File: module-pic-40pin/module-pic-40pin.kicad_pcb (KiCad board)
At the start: 2 copper layers, 93 x 61.9 mm, 21 parts, among them J1 input_power, J2 ANALOG, J3 icsp, J4 PORTB, J5 PORTC, J6 Conn_02x04_Odd_Even, J7 RB0_CONN, J8 PORTD, SW1 reset, SW2 EXT_INT0, U1 PIC16F877A-IP, Y1 20MHz

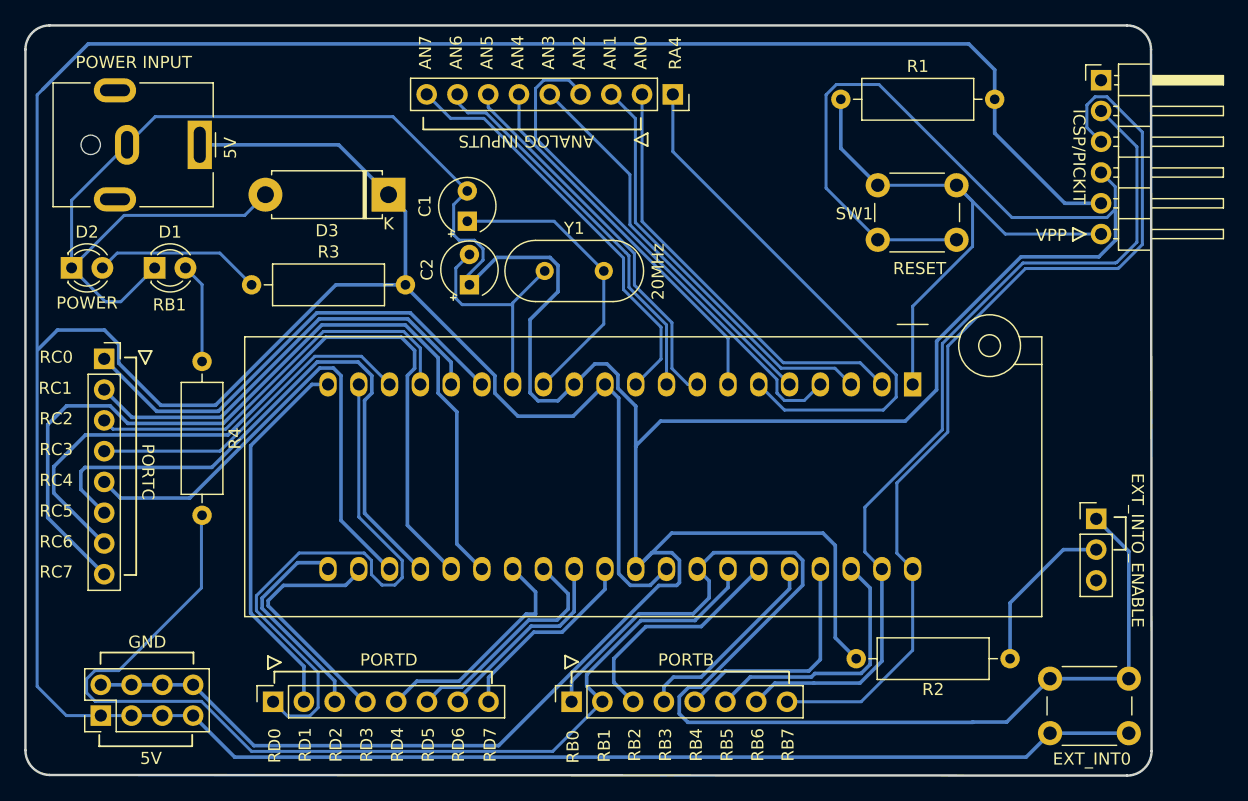
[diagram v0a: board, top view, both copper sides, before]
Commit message: update module-pic-40pin layout - v1.2
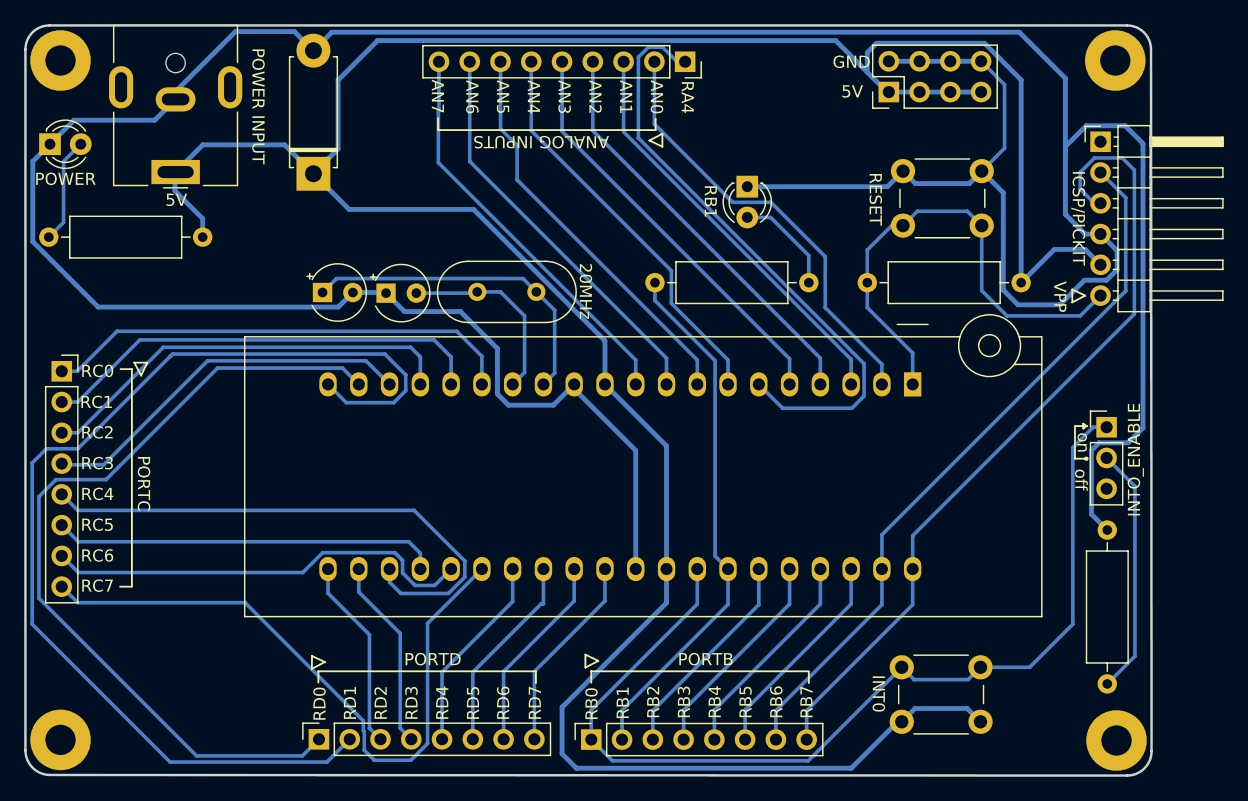
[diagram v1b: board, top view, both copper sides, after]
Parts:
- added REF**: MountingHole_2.5mm_Pad, MountingHole:MountingHole_2.5mm_Pad, F.Cu at (107.8, 69.6)
- added REF**: MountingHole_2.5mm_Pad, MountingHole:MountingHole_2.5mm_Pad, F.Cu at (195.0, 125.8)
- added REF**: MountingHole_2.5mm_Pad, MountingHole:MountingHole_2.5mm_Pad, F.Cu at (194.9, 69.6)
- added REF**: MountingHole_2.5mm_Pad, MountingHole:MountingHole_2.5mm_Pad, F.Cu at (107.8, 125.7)
- moved J6 83.0 mm to (176.2, 72.3)
- moved R4 50.5 mm to (169.6, 88.0), turned to 180 degrees
- moved D1 49.4 mm to (164.5, 80.1), turned to -90 degrees
- moved R3 17.2 mm to (106.8, 84.2)
- moved R1 15.3 mm to (174.4, 88.0)
- moved C1 13.3 mm to (129.4, 88.8), turned to 0 degrees
- moved SW2 12.3 mm to (177.2, 119.7)
- moved D2 10.4 mm to (106.9, 76.6)
- moved R2 8.29 mm to (194.2, 121.1), turned to 90 degrees
- moved J7 7.61 mm to (194.2, 99.9)
- moved SW1 7.19 mm to (177.3, 78.8), turned to 0 degrees
- moved C2 6.92 mm to (134.7, 88.8), turned to 0 degrees
- moved D3 6.43 mm to (128.7, 79.0), turned to 90 degrees
- moved Y1 5.83 mm to (142.2, 88.7)
- moved J3 5.08 mm to (193.6, 76.4)
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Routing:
- net +5V: track 348.2 -> 232.3 mm
- net /RD1: track 31.4 -> 89.0 mm
- net /RB1: track 85.0 -> 43.8 mm
- net GND: track 321.9 -> 293.8 mm
- net /RC6: track 62.5 -> 35.7 mm
- net /RD0: track 48.8 -> 68.8 mm
- net /RC5: track 50.5 -> 31.9 mm
- net /RB0: track 99.4 -> 81.8 mm
- net /RC7: track 71.2 -> 54.3 mm
- net /RB6: track 72.8 -> 59.6 mm
- net /RB7: track 77.9 -> 67.1 mm
- net /AN2: track 42.4 -> 34.4 mm
- net Net-(J7-Pad2): track 13.5 -> 20.6 mm
- net /VPP: track 47.5 -> 40.6 mm
- net Net-(D2-Pad2): track 13.9 -> 8.76 mm
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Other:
- board text added: "INT0"
- board text added: "INTO_ENABLE"
- board text added: "off"
- board text added: "on"
- board text removed: "EXT_INT0"
- board text removed: "EXT_INTO_ENABLE"

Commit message: update module-pic-40pin
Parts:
- added G***: LOGO, footprints:ladesi, F.Cu at (115.3, 120.1)
- added REF**: KiCad-Logo, Symbol:KiCad-Logo2_5mm_SilkScreen, F.Cu at (151.9, 81.1)
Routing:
- net /AN0: track 36.3 -> 37.7 mm

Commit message: update module-pic-40pin
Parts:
- moved R4 59.1 mm to (123.9, 50.6)
- moved Y1 59.1 mm to (96.5, 51.4)
- moved C2 59.1 mm to (89.0, 51.5)
- moved R3 59.1 mm to (61.1, 46.8)
- moved REF** 59.1 mm to (62.1, 32.3)
- moved REF** 59.1 mm to (62.1, 88.3)
- moved C1 59.1 mm to (83.7, 51.4)
- moved D1 59.1 mm to (118.8, 42.7)
- moved D2 59.1 mm to (61.2, 39.2)
- moved D3 59.1 mm to (83.0, 41.6)
- moved G*** 59.1 mm to (69.6, 82.7)
- moved J1 59.1 mm to (71.6, 41.5)
- moved J2 59.1 mm to (113.6, 32.4)
- moved J3 59.1 mm to (147.9, 39.0)
- moved J6 59.1 mm to (130.5, 34.9)
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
